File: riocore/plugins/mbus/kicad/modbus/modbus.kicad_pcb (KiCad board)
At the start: 2 copper layers, 12 x 19.5 mm, 6 parts, among them U12 MAX485E

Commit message: kicad: module selection / some fixes
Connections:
- net /rw renamed /tx_enable
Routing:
- net /tx_enable: track 0.00 -> 1.27 mm
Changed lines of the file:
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@@
 	(net 4 "Net-(U12-B)")
 	(net 5 "/rx")
-	(net 6 "/rw")
+	(net 6 "/tx_enable")
 	(net 7 "/tx")
 	(footprint "Package_SO:Diodes_SO-8EP"
@@
 			(size 1.505 0.802)
 			(layers "F.Cu" "F.Mask" "F.Paste")
-			(net 6 "/rw")
+			(net 6 "/tx_enable")
 			(pinfunction "~{RE}")
 			(pintype "input")
@@
 			(size 1.505 0.802)
 			(layers "F.Cu" "F.Mask" "F.Paste")
-			(net 6 "/rw")
+			(net 6 "/tx_enable")
 			(pinfunction "DE")
 			(pintype "input")
@@
 		(net 4)
 	)
+	(segment
+		(start 145.96 95.495)
+		(end 147.23 95.495)
+		(width 0.2)
+		(layer "F.Cu")
+		(net 6)
+	)
 	(embedded_fonts no)

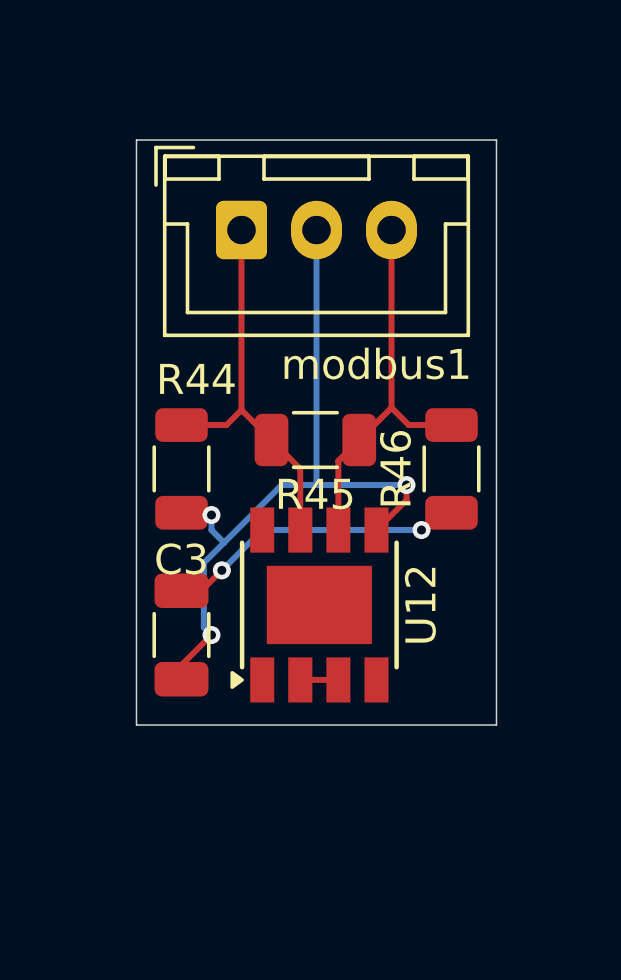
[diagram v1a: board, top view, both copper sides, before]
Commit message: modbus: kicad: iso
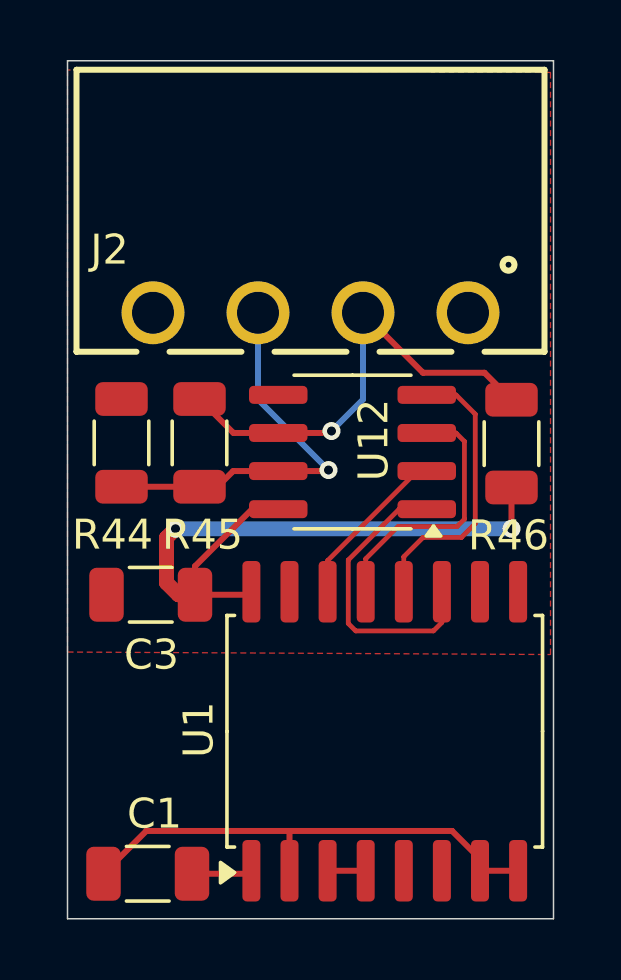
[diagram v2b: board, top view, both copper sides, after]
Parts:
- removed modbus1: Conn_01x03, Connector_JST:JST_XH_B3B-XH-A_1x03_P2.50mm_Vertical
- added C1: 100n, Capacitor_SMD:C_1206_3216Metric, F.Cu at (140.9, 102.0)
- added J2: modbus, kicad-lbr:691322110004, F.Cu at (146.3, 83.3)
- added U1: ADuM1411, Package_SO:SOIC-16W_7.5x10.3mm_P1.27mm, F.Cu at (148.8, 97.2)
- U12: footprint Package_SO:Diodes_SO-8EP -> Package_SO:SOIC-8_3.9x4.9mm_P1.27mm
- moved U12 5.22 mm to (147.7, 87.9), turned to 180 degrees
- moved R45 3.86 mm to (142.6, 87.6), turned to -90 degrees
- moved R44 2.18 mm to (140.0, 87.6), turned to 90 degrees
- moved R46 2.17 mm to (153.0, 87.6)
- moved C3 1.69 mm to (141.0, 92.7), turned to 180 degrees
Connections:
- net 3v3 renamed F_5V
- net gnd renamed F_GND
- U12 pad 1: /rx -> Net-(U1-VID)
- U12 pad 2: /tx_enable -> Net-(U1-VOA)
- U12 pad 3: /tx_enable -> Net-(U1-VOB)
- U12 pad 4: /tx -> Net-(U1-VOC)
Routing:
- net F_GND: track 24.9 -> 0.40 mm, vias 3 -> 0
- net GND: track 0.00 -> 16.5 mm
- net F_5V: track 10.1 -> 22.0 mm
- net Net-(U1-VID): track 0.00 -> 9.80 mm
- net Net-(U1-VOC): track 0.00 -> 9.54 mm
- net Net-(U1-VOB): track 0.00 -> 8.90 mm
- net Net-(U1-VOA): track 0.00 -> 5.58 mm
- net Net-(U12-A): track 13.0 -> 15.4 mm, vias 0 -> 1
- net +3.3V: track 0.00 -> 2.02 mm
- net Net-(U12-B): track 13.0 -> 13.4 mm, vias 0 -> 1
- added copper zone on F.Cu, net F_GND
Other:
- board size 12 x 19.5 mm -> 16.2 x 28.6 mm

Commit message: some changes
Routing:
- net F_GND: track 0.40 -> 33.2 mm
- net Net-(U12-A): track 15.4 -> 14.4 mm, vias 1 -> 0
- removed copper zone on F.Cu, net F_GND
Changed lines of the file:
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@@
 	)
 	(segment
-		(start 151.95 92.5575)
+		(start 138.824 87.3085)
+		(end 138.824 91.9815)
+		(width 0.2)
+		(layer "F.Cu")
+		(net 2)
+	)
+	(segment
+		(start 138.824 91.9815)
+		(end 139.5 92.6575)
+		(width 0.2)
+		(layer "F.Cu")
+		(net 2)
+	)
+	(segment
+		(start 140 86.1325)
+		(end 138.824 87.3085)
+		(width 0.2)
+		(layer "F.Cu")
+		(net 2)
+	)
+	(segment
+		(start 150.659968 94.2445)
 		(end 151.95 92.954468)
 		(width 0.2)
@@
 	)
 	(segment
-		(start 146.935 87.265)
-		(end 147 87.2)
-		(width 0.2)
-		(layer "F.Cu")
-		(net 3)
+		(start 140 86.1325)
+		(end 141.05 85.0825)
+		(width 0.2)
+		(layer "F.Cu")
+		(net 2)
+	)
+	(segment
+		(start 153.22 92.5575)
+		(end 151.95 92.5575)
+		(width 0.2)
+		(layer "F.Cu")
+		(net 2)
+	)
+	(segment
+		(start 145.6 92.954468)
+		(end 145.6 92.5575)
+		(width 0.2)
+		(layer "F.Cu")
+		(net 2)
+	)
+	(segment
+		(start 143.73 84.5)
+		(end 142.2925 84.5)
+		(width 0.2)
+		(layer "F.Cu")
+		(net 2)
+	)
+	(segment
+		(start 139.5 92.6575)
+		(end 140.726 93.8835)
+		(width 0.2)
+		(layer "F.Cu")
+		(net 2)
+	)
+	(segment
+		(start 141.05 85.0825)
+		(end 141.05 83.2575)
+		(width 0.2)
+		(layer "F.Cu")
+		(net 2)
+	)
+	(segment
+		(start 145.6 92.5575)
+		(end 145.6 93.582499)
+		(width 0.2)
+		(layer "F.Cu")
+		(net 2)
+	)
+	(segment
+		(start 151.95 92.954468)
+		(end 151.95 92.5575)
+		(width 0.2)
+		(layer "F.Cu")
+		(net 2)
+	)
+	(segment
+		(start 146.262001 94.2445)
+		(end 150.659968 94.2445)
+		(width 0.2)
+		(layer "F.Cu")
+		(net 2)
+	)
+	(segment
+		(start 142.2925 84.5)
+		(end 141.05 83.2575)
+		(width 0.2)
+		(layer "F.Cu")
+		(net 2)
+	)
+	(segment
+		(start 145.225 85.995)
+		(end 143.73 84.5)
+		(width 0.2)
+		(layer "F.Cu")
+		(net 2)
+	)
+	(segment
+		(start 140.726 93.8835)
+		(end 144.670968 93.8835)
+		(width 0.2)
+		(layer "F.Cu")
+		(net 2)
+	)
+	(segment
+		(start 144.670968 93.8835)
+		(end 145.6 92.954468)
+		(width 0.2)
+		(layer "F.Cu")
+		(net 2)
+	)
+	(segment
+		(start 145.6 93.582499)
+		(end 146.262001 94.2445)
+		(width 0.2)
+		(layer "F.Cu")
+		(net 2)
 	)
 	(segment
 		(start 152.1 85.2575)
-		(end 150.05 85.2575)
-		(width 0.2)
-		(layer "F.Cu")
-		(net 3)
-	)
-	(segment
-		(start 152.1 85.2575)
-		(end 153 86.1575)
+		(end 148.0575 85.2575)
+		(width 0.2)
+		(layer "F.Cu")
+		(net 3)
+	)
+	(segment
+		(start 148.05 85.25)
+		(end 148.05 83.2575)
+		(width 0.2)
+		(layer "F.Cu")
+		(net 3)
+	)
+	(segment
+		(start 153 86.1575)
+		(end 152.1 85.2575)
+		(width 0.2)
+		(layer "F.Cu")
+		(net 3)
+	)
+	(segment
+		(start 148.0575 85.2575)
+		(end 148.05 85.25)
+		(width 0.2)
+		(layer "F.Cu")
+		(net 3)
+	)
+	(segment
+		(start 148.05 85.75)
+		(end 148.05 85.25)
 		(width 0.2)
 		(layer "F.Cu")
@@
 	(segment
 		(start 145.225 87.265)
-		(end 146.935 87.265)
+		(end 146.535 87.265)
 		(width 0.2)
 		(layer "F.Cu")
@@
 	)
 	(segment
+		(start 146.535 87.265)
+		(end 148.05 85.75)
+		(width 0.2)
+		(layer "F.Cu")
+		(net 3)
+	)
+	(segment
 		(start 143.7325 87.265)
 		(end 145.225 87.265)
 		(width 0.2)
 		(layer "F.Cu")
-		(net 3)
-	)
-	(segment
-		(start 150.05 85.2575)
-		(end 148.05 83.2575)
-		(width 0.2)
-		(layer "F.Cu")
-		(net 3)
-	)
-	(via
-		(at 147 87.2)
-		(size 0.6)
-		(drill 0.3)
-		(layers "F.Cu" "B.Cu")
-		(net 3)
-	)
-	(segment
-		(start 147 87.2)
-		(end 148.05 86.15)
-		(width 0.2)
-		(layer "B.Cu")
-		(net 3)
-	)
-	(segment
-		(start 148.05 86.15)
-		(end 148.05 83.2575)
-		(width 0.2)
-		(layer "B.Cu")
 		(net 3)
 	)
@@
 		(net 13)
 	)
-	(zone
-		(net 2)
-		(net_name "F_GND")
-		(layer "F.Cu")
-		(hatch edge 0.5)
-		(connect_pads
-			(clearance 0.16)
-		)
-		(min_thickness 0.16)
-		(filled_areas_thickness no)
-		(fill yes
-			(thermal_gap 0.5)
-			(thermal_bridge_width 0.5)
-		)
-		(polygon
-			(pts
-				(xy 154.3 75.247708) (xy 138.2 75.164718) (xy 138.2 94.567293) (xy 154.3 94.650283)
-			)
-		)
-	)
 	(embedded_fonts no)
